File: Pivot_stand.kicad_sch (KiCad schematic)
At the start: 6 parts, among them J1 USB_B_Micro, J2 Conn_01x02_Male, U1 TLV1117-33

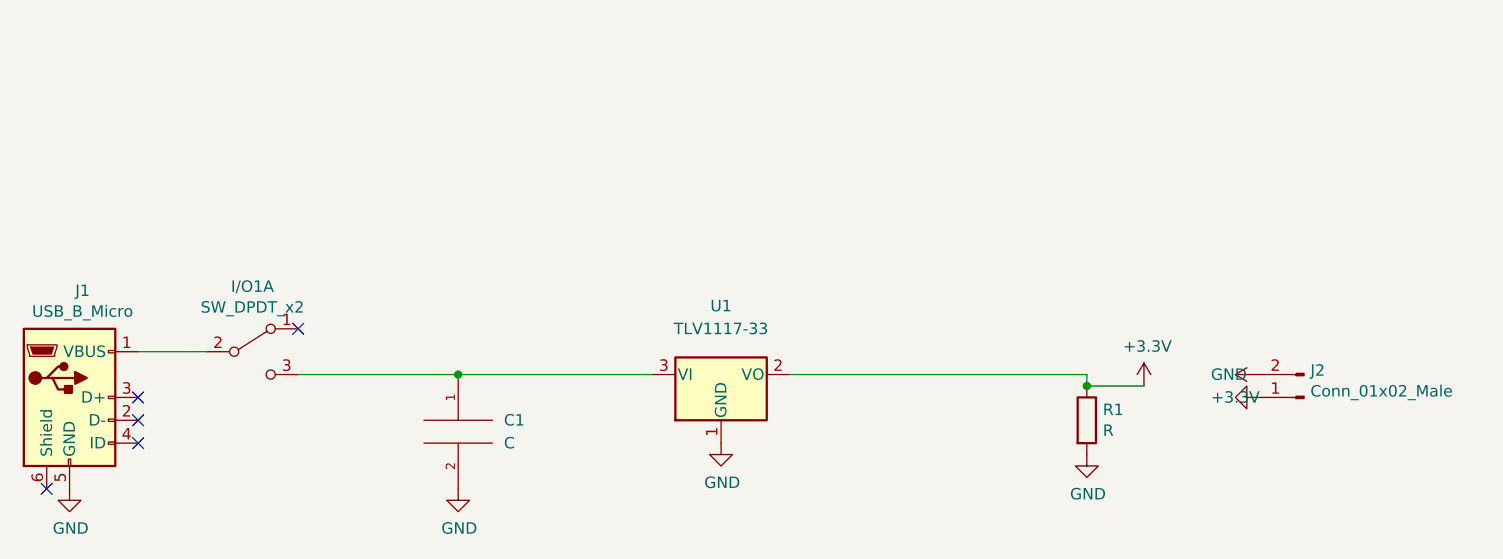
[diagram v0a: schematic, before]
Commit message: Updated format to KiCad 6
Updated format to KiCad 6
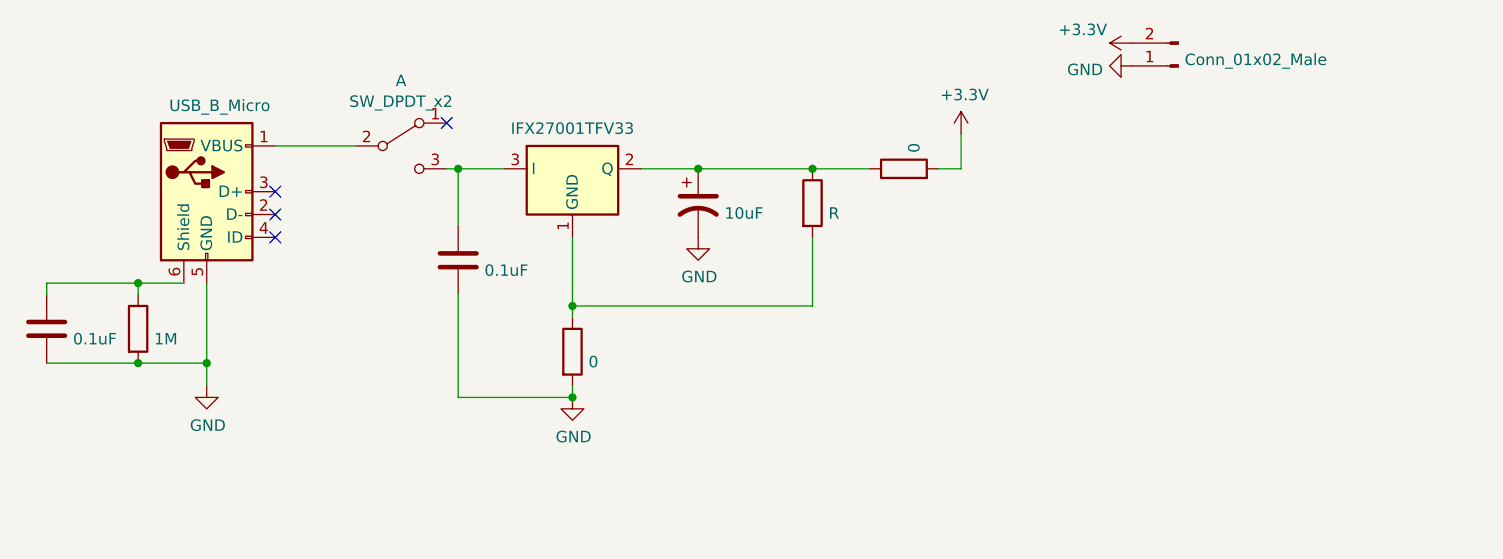
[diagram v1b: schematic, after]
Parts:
- removed C1: C, BadgePirates:C_0805_2012Metric, symbol pspice:C
- removed U1: TLV1117-33, BadgePirates:SOT-223, symbol Regulator_Linear:TLV1117-33
- added ?: IFX27001TFV33, Package_TO_SOT_SMD:TO-252-3_TabPin2, symbol Regulator_Linear:IFX27001TFV33
- added ?: 10uF, Capacitor_SMD:C_0805_2012Metric, symbol Pivot_stand-rescue:CP1-Device
- added ? (x2): 0, Resistor_SMD:R_1206_3216Metric, symbol Pivot_stand-rescue:R-Device
- added ?: 1M, Resistor_SMD:R_0603_1608Metric_Pad1.05x0.95mm_HandSolder, symbol Pivot_stand-rescue:R-Device
- added ? (x2): 0.1uF, Capacitor_SMD:C_0805_2012Metric_Pad1.18x1.45mm_HandSolder, symbol Pivot_stand-rescue:C-Device
- ?: renamed from J1; footprint BadgePirates:USB_Micro-B_Wuerth_629105150521_fgFixed -> Connector_USB:USB_Micro-B_Wuerth_629105150521; symbol Connector:USB_B_Micro -> Pivot_stand-rescue:USB_B_Micro-Connector
- ?: renamed from R1; symbol Device:R -> Pivot_stand-rescue:R-Device
- ?: renamed from J2; symbol Connector:Conn_01x02_Male -> Pivot_stand-rescue:Conn_01x02_Male-Connector
- ?: renamed from I/O1; footprint BadgePirates:SW_SPDT_PCM12 -> Button_Switch_SMD:SW_SPDT_CK-JS102011SAQN
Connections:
- net +3V3: now also ?.2; no longer ?.1
- net GND: now also ?.2, ?.2, ?.2, ?.2, ?.2; no longer ?.2
- net at ?.6 (Shield): now also ?.1, ?.1
- net at ?.3 (C): now also ?.1, ?.3 (I)
- new net: ?.1, ?.1 (GND), ?.2
- new net: ?.1, ?.1, ?.1, ?.2 (Q)
- no-connect marks 5 -> 4
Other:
- company: BadgePirates LLC -> (none)
- title: Desktop Badge Stand -> (none)
- moved on the sheet: A

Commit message: Changed the regulator symbol
Changed the regulator symbol to include a 4th pin for the output tab.
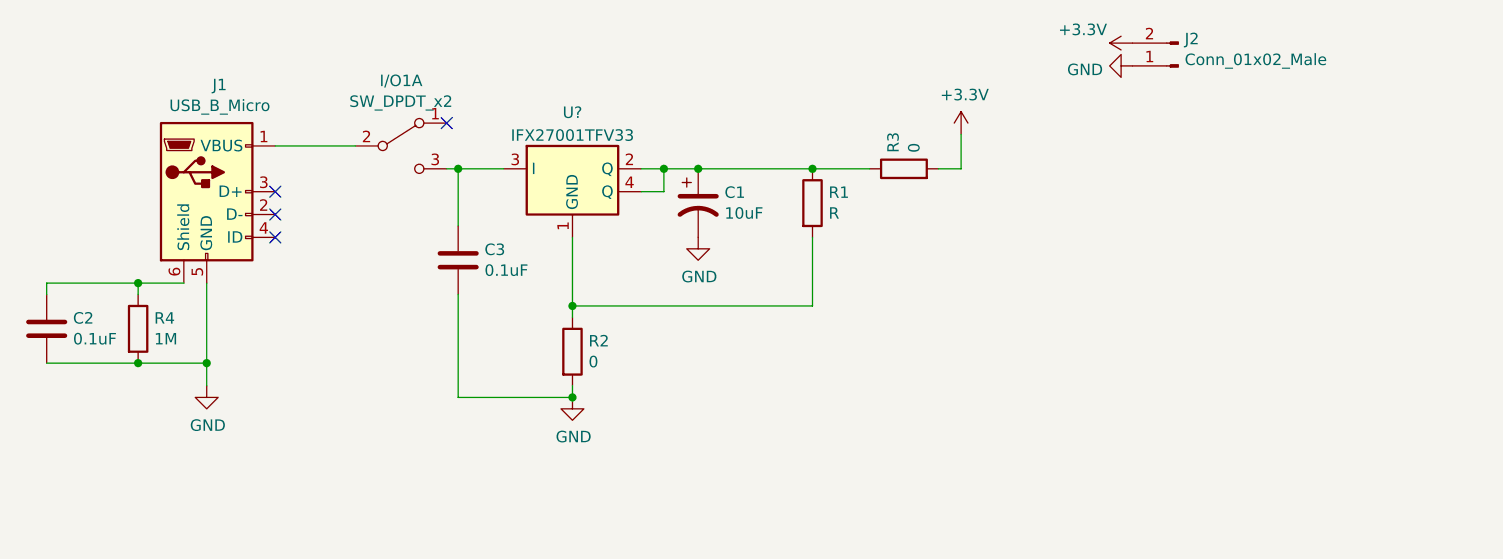
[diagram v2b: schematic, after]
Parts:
- removed ?: IFX27001TFV33, Package_TO_SOT_SMD:TO-252-3_TabPin2, symbol Regulator_Linear:IFX27001TFV33
- added U?: IFX27001TFV33, Package_TO_SOT_SMD:TO-252-3_TabPin2, symbol BadgePiratesSymbolLibrary:IFX27001TFV33
- gave numbers to parts that had none: 10
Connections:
- net at R1.2, R2.1: now also U?.1 (GND)
- net at C1.1, R1.1, R3.1: now also U?.2 (Q), U?.4 (Q)
- net at C3.1, I/O1.3 (C): now also U?.3 (I)
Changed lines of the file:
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@@
   (junction (at 167.64 68.58) (diameter 0) (color 0 0 0 0)
+  )
+  (junction (at 163.83 68.58) (diameter 0) (color 0 0 0 0)
   )
   (junction (at 153.67 93.98) (diameter 0) (color 0 0 0 0)
@@
     (stroke (width 0) (type default) (color 0 0 0 0))
   )
+  (wire (pts (xy 161.29 71.12) (xy 163.83 71.12))
+    (stroke (width 0) (type default) (color 0 0 0 0))
+  )
   (wire (pts (xy 180.34 83.82) (xy 153.67 83.82))
     (stroke (width 0) (type default) (color 0 0 0 0))
@@
     (stroke (width 0) (type default) (color 0 0 0 0))
   )
+  (wire (pts (xy 163.83 68.58) (xy 163.83 71.12))
+    (stroke (width 0) (type default) (color 0 0 0 0))
+  )
   (wire (pts (xy 105.41 81.28) (xy 105.41 82.55))
     (stroke (width 0) (type default) (color 0 0 0 0))
@@
     (stroke (width 0) (type default) (color 0 0 0 0))
   )
-  (wire (pts (xy 161.29 68.58) (xy 167.64 68.58))
+  (wire (pts (xy 161.29 68.58) (xy 163.83 68.58))
     (stroke (width 0) (type default) (color 0 0 0 0))
   )
@@
     (stroke (width 0) (type default) (color 0 0 0 0))
   )
+  (wire (pts (xy 163.83 68.58) (xy 167.64 68.58))
+    (stroke (width 0) (type default) (color 0 0 0 0))
+  )
   (symbol (lib_id "Pivot_stand-rescue:USB_B_Micro-Connector") (at 113.03 71.12 0) (unit 1)
     (in_bom yes) (on_board yes)
-    (property "Reference" "" (id 0) (at 114.4778 59.2582 0))
+    (property "Reference" "J1" (id 0) (at 114.4778 59.2582 0))
     (property "Value" "USB_B_Micro" (id 1) (at 114.4778 61.5696 0))
     (property "Footprint" "Connector_USB:USB_Micro-B_Wuerth_629105150521" (id 2) (at 116.84 72.39 0)
@@
     (pin "1")
   )
-  (symbol (lib_id "Regulator_Linear:IFX27001TFV33") (at 153.67 68.58 0) (unit 1)
-    (in_bom yes) (on_board yes)
-    (property "Reference" "" (id 0) (at 153.67 61.7982 0))
-    (property "Value" "IFX27001TFV33" (id 1) (at 153.67 64.1096 0))
-    (property "Footprint" "Package_TO_SOT_SMD:TO-252-3_TabPin2" (id 2) (at 153.67 69.85 0)
-      (effects (font (size 1.27 1.27)) hide)
-    )
-    (property "Datasheet" "https://static6.arrow.com/aropdfconversion/dc75757ae45a88e5f69bdce3f2a651a5fe0ca07d/ifx27001_ds_10.pdf" (id 3) (at 153.67 69.85 0)
-      (effects (font (size 1.27 1.27)) hide)
-    )
-    (pin "1")
-    (pin "2")
-    (pin "3")
-  )
   (symbol (lib_id "power:GND") (at 153.67 93.98 0) (unit 1)
     (in_bom yes) (on_board yes)
@@
   (symbol (lib_id "Pivot_stand-rescue:CP1-Device") (at 167.64 72.39 0) (unit 1)
     (in_bom yes) (on_board yes)
-    (property "Reference" "" (id 0) (at 170.561 71.2216 0)
+    (property "Reference" "C1" (id 0) (at 170.561 71.2216 0)
       (effects (font (size 1.27 1.27)) (justify left))
     )
@@
   (symbol (lib_id "Pivot_stand-rescue:R-Device") (at 180.34 72.39 0) (unit 1)
     (in_bom yes) (on_board yes)
-    (property "Reference" "" (id 0) (at 182.118 71.2216 0)
+    (property "Reference" "R1" (id 0) (at 182.118 71.2216 0)
       (effects (font (size 1.27 1.27)) (justify left))
     )
@@
   (symbol (lib_id "Pivot_stand-rescue:Conn_01x02_Male-Connector") (at 220.98 57.15 180) (unit 1)
     (in_bom yes) (on_board yes)
-    (property "Reference" "" (id 0) (at 221.6912 54.1528 0)
+    (property "Reference" "J2" (id 0) (at 221.6912 54.1528 0)
       (effects (font (size 1.27 1.27)) (justify right))
     )
@@
   (symbol (lib_id "Switch:SW_DPDT_x2") (at 134.62 66.04 0) (unit 1)
     (in_bom yes) (on_board yes)
-    (property "Reference" "" (id 0) (at 134.62 58.801 0))
+    (property "Reference" "I/O1" (id 0) (at 134.62 58.801 0))
     (property "Value" "SW_DPDT_x2" (id 1) (at 134.62 61.1124 0))
     (property "Footprint" "Button_Switch_SMD:SW_SPDT_CK-JS102011SAQN" (id 2) (at 134.62 66.04 0)
@@
   (symbol (lib_id "Pivot_stand-rescue:R-Device") (at 153.67 88.9 0) (unit 1)
     (in_bom yes) (on_board yes)
-    (property "Reference" "" (id 0) (at 155.448 87.7316 0)
+    (property "Reference" "R2" (id 0) (at 155.448 87.7316 0)
       (effects (font (size 1.27 1.27)) (justify left))
     )
@@
   (symbol (lib_id "Pivot_stand-rescue:R-Device") (at 190.5 68.58 90) (unit 1)
     (in_bom yes) (on_board yes)
-    (property "Reference" "" (id 0) (at 189.3316 66.802 0)
+    (property "Reference" "R3" (id 0) (at 189.3316 66.802 0)
       (effects (font (size 1.27 1.27)) (justify left))
     )
@@
   (symbol (lib_id "Pivot_stand-rescue:R-Device") (at 105.41 86.36 0) (unit 1)
     (in_bom yes) (on_board yes)
-    (property "Reference" "" (id 0) (at 107.188 85.1916 0)
+    (property "Reference" "R4" (id 0) (at 107.188 85.1916 0)
       (effects (font (size 1.27 1.27)) (justify left))
     )
@@
   (symbol (lib_id "Pivot_stand-rescue:C-Device") (at 95.25 86.36 0) (unit 1)
     (in_bom yes) (on_board yes)
-    (property "Reference" "" (id 0) (at 98.171 85.1916 0)
+    (property "Reference" "C2" (id 0) (at 98.171 85.1916 0)
       (effects (font (size 1.27 1.27)) (justify left))
     )
@@
   (symbol (lib_id "Pivot_stand-rescue:C-Device") (at 140.97 78.74 0) (unit 1)
     (in_bom yes) (on_board yes)
-    (property "Reference" "" (id 0) (at 143.891 77.5716 0)
+    (property "Reference" "C3" (id 0) (at 143.891 77.5716 0)
       (effects (font (size 1.27 1.27)) (justify left))
     )
@@
     (pin "1")
     (pin "2")
+  )
+  (symbol (lib_id "BadgePiratesSymbolLibrary:IFX27001TFV33") (at 153.67 68.58 0) (unit 1)
+    (in_bom yes) (on_board yes) (fields_autoplaced)
+    (property "Reference" "U?" (id 0) (at 153.67 62.3402 0))
+    (property "Value" "IFX27001TFV33" (id 1) (at 153.67 64.8771 0))
+    (property "Footprint" "Package_TO_SOT_SMD:TO-252-3_TabPin2" (id 2) (at 153.67 69.85 0)
+      (effects (font (size 1.27 1.27)) hide)
+    )
+    (property "Datasheet" "https://static6.arrow.com/aropdfconversion/dc75757ae45a88e5f69bdce3f2a651a5fe0ca07d/ifx27001_ds_10.pdf" (id 3) (at 153.67 69.85 0)
+      (effects (font (size 1.27 1.27)) hide)
+    )
+    (pin "1")
+    (pin "2")
+    (pin "3")
+    (pin "4")
   )
   (sheet_instances
@@
       (reference "R4") (unit 1) (value "1M") (footprint "Resistor_SMD:R_0603_1608Metric_Pad1.05x0.95mm_HandSolder")
     )
-    (path "/00000000-0000-0000-0000-000060e3d2a8"
-      (reference "U1") (unit 1) (value "IFX27001TFV33") (footprint "Package_TO_SOT_SMD:TO-252-3_TabPin2")
-    )
-  )
+    (path "/27f176fa-5907-47fa-b2d2-85c41dd0f18b"
+      (reference "U?") (unit 1) (value "IFX27001TFV33") (footprint "Package_TO_SOT_SMD:TO-252-3_TabPin2")
+    )
+  )
